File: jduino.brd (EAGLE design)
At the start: 100 x 80 mm, 20 parts, among them IC1 7805T, IC2 ATMEGA48/88/168-PU, Q1 16 mHz

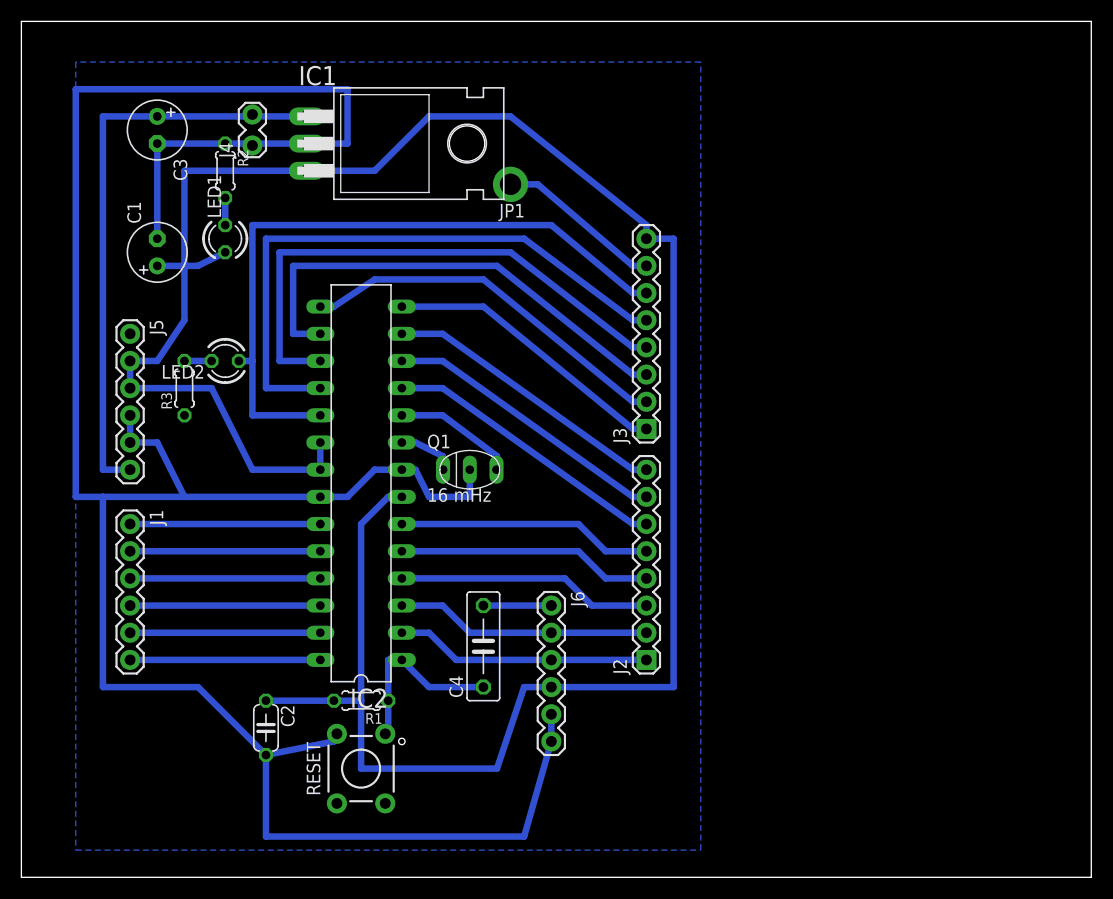
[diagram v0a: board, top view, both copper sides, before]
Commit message: Added power elements.
Added a protection diode and a power switch. Also swapped out the
7805 for a LDO regulator.
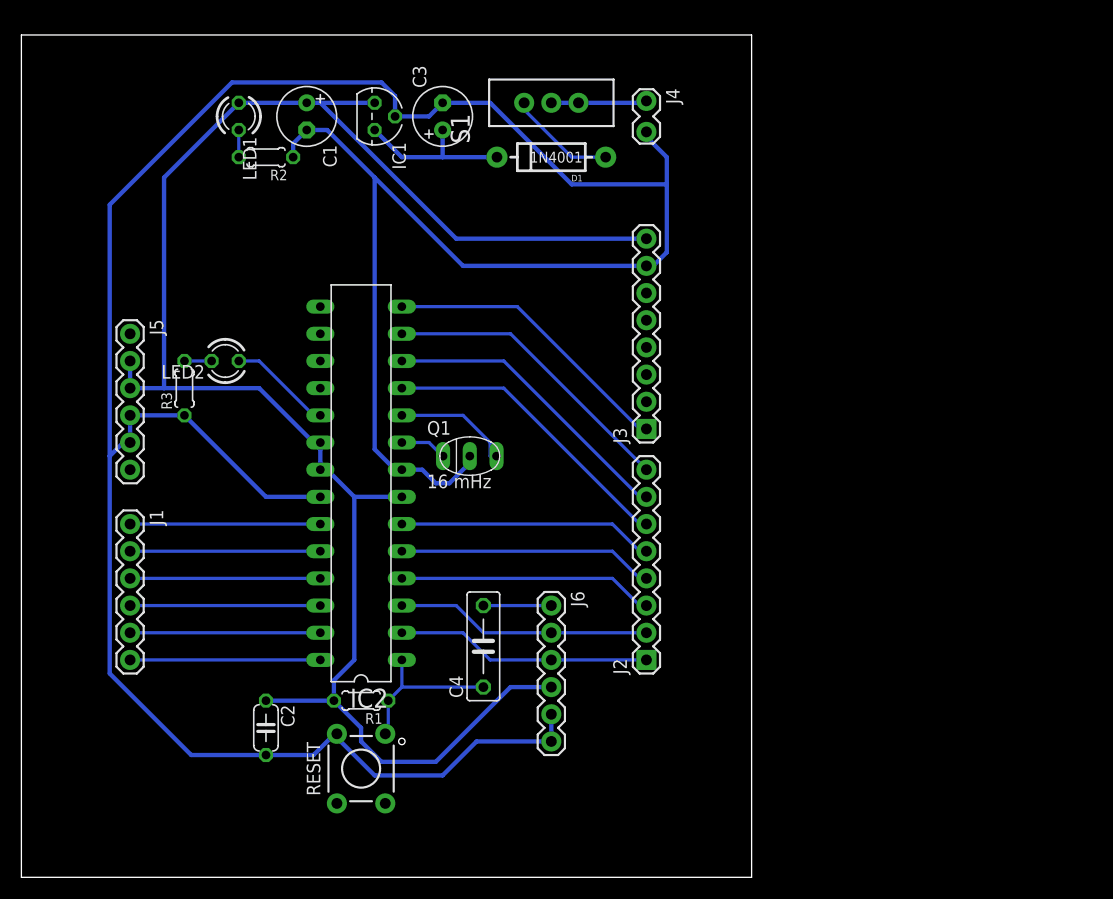
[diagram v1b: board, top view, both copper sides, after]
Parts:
- removed JP1: M01PTH_2MM, SparkFun:1X01_2MM
- added D1: 1N4001, SparkFun-DiscreteSemi:DIODE-1N4001
- added S1: power, SparkFun-Electromechanical:SWITCH-SPDT
- IC1: value 7805T -> LM2936Z-5.0; device linear:TO220H -> national-semiconductor:TO92
- J4: value (none) -> 6V - 30V in
- R2: value 330ohm -> 330
- moved J4 37.0 mm to (58.4, 72.4), turned to 270 degrees
- moved C3 26.7 mm to (39.4, 71.1), turned to 90 degrees
- moved C1 18.9 mm to (26.7, 71.1), turned to 270 degrees
- moved LED1 11.5 mm to (20.3, 71.1), turned to 270 degrees
- moved IC1 4.58 mm to (33.0, 71.1)
- moved R2 4.02 mm to (22.9, 67.3), turned to 180 degrees
- moved Q1 1.27 mm to (41.9, 39.4)
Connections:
- new net N$6: C3.+, D1.C, IC1.3
- new net N$7: D1.A, S1.1
- net +5V: now also IC1.1; no longer IC1.3
- net GND: now also J3.7, J4.2; no longer J4.1
- net N$1: now also J5.1
- net N$2: now also J4.1, S1.2, S1.3; no longer J3.7, JP1.1
- net VIN: no longer C3.+, IC1.1, J4.2
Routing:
- net D12: track 57.2 -> 0.00 mm
- net +5V: track 221.2 -> 164.7 mm
- net D13: track 64.5 -> 9.72 mm
- net VIN: track 54.8 -> 0.00 mm
- net D11: track 51.3 -> 0.00 mm
- net D10: track 45.5 -> 0.00 mm
- net GND: track 234.6 -> 275.2 mm
- net D9: track 35.3 -> 0.00 mm
- net N$6: track 0.00 -> 15.0 mm
- net N$7: track 0.00 -> 10.1 mm
- net N$2: track 15.5 -> 9.07 mm
- net RESET: track 16.9 -> 15.1 mm
- net D6: track 26.9 -> 28.1 mm
- net D5: track 26.9 -> 28.1 mm
- net D7: track 26.9 -> 28.1 mm
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- removed copper zone on layer 16, net GND
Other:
- board size 100 x 80 mm -> 68.2 x 78.7 mm

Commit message: Initial complete version.
Routed D9 - D13, GND, and AREF to the headers. Rotated the FTDI
header to be able to use a right angle header. Two jumpers remain.
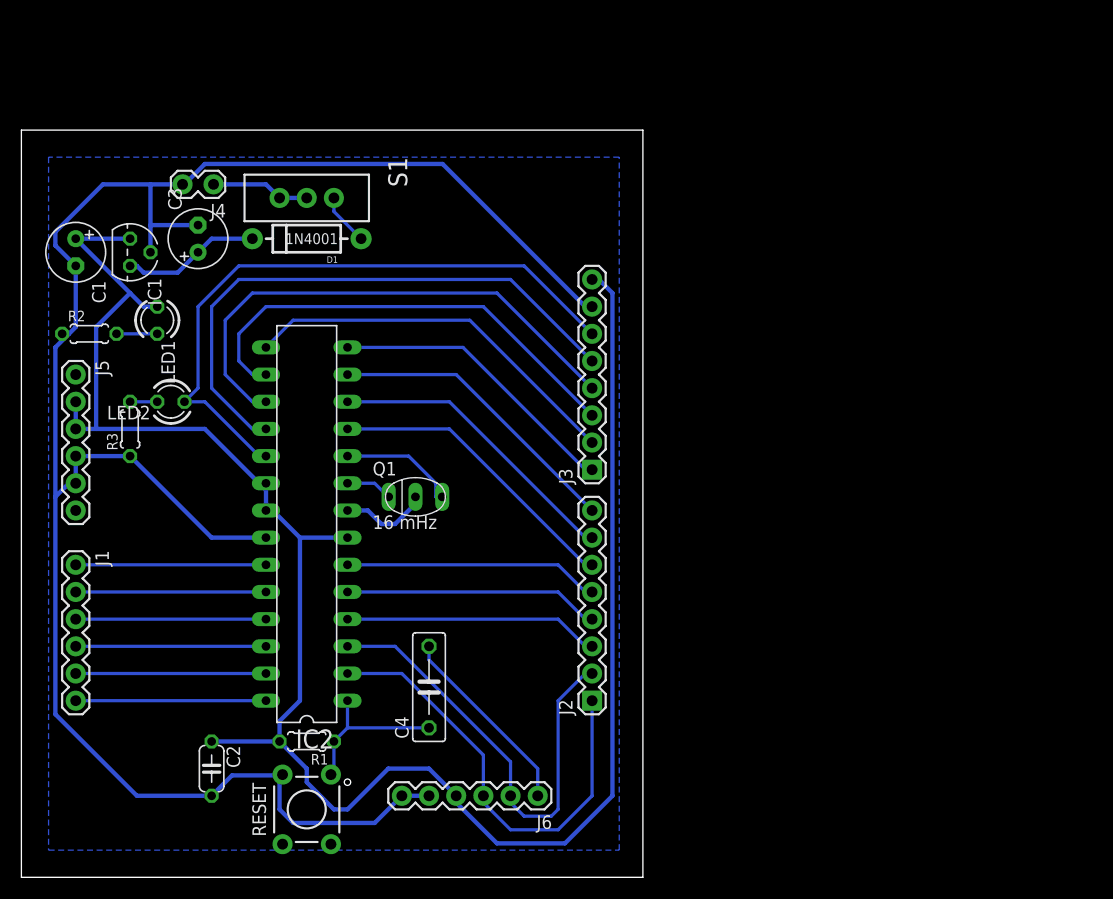
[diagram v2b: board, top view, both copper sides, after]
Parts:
- moved J4 41.3 mm to (17.8, 64.8), turned to 180 degrees
- moved IC1 26.2 mm to (10.2, 58.4)
- moved C3 25.6 mm to (16.5, 59.7)
- moved C1 25.0 mm to (5.08, 58.4)
- moved S1 24.5 mm to (26.7, 63.5), turned to 270 degrees
- moved D1 24.1 mm to (26.7, 59.7)
- moved R2 23.3 mm to (6.35, 50.8), turned to 0 degrees
- moved LED1 20.5 mm to (12.7, 52.1)
- moved J6 17.8 mm to (48.3, 7.62), turned to 180 degrees
- moved J1 6.35 mm to (5.08, 29.2)
- moved R3 6.35 mm to (10.2, 41.9)
- moved R1 6.35 mm to (26.7, 12.7)
- moved C2 6.35 mm to (17.8, 10.2)
- moved RESET 6.35 mm to (26.7, 6.35)
- moved C4 6.35 mm to (38.1, 17.8)
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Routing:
- net GND: track 275.2 -> 196.0 mm
- net D12: track 0.00 -> 54.0 mm
- net D13: track 9.72 -> 60.2 mm
- net D11: track 0.00 -> 49.0 mm
- net D10: track 0.00 -> 43.9 mm
- net D9: track 0.00 -> 36.3 mm
- net D1: track 23.9 -> 43.1 mm
- net D0: track 23.9 -> 41.7 mm
- net +5V: track 164.7 -> 180.3 mm
- net N$1: track 6.35 -> 18.2 mm
- net N$7: track 10.1 -> 4.86 mm
- net N$6: track 15.0 -> 13.0 mm
- net N$26: track 2.54 -> 3.81 mm
- added copper zone on layer 16, net GND
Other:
- board size 68.2 x 78.7 mm -> 58.1 x 69.8 mm

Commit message: Replaced Euro-stype capacitors.
Replaced the large reset capacitors with smaller-package 0.1 uF
capacitors.
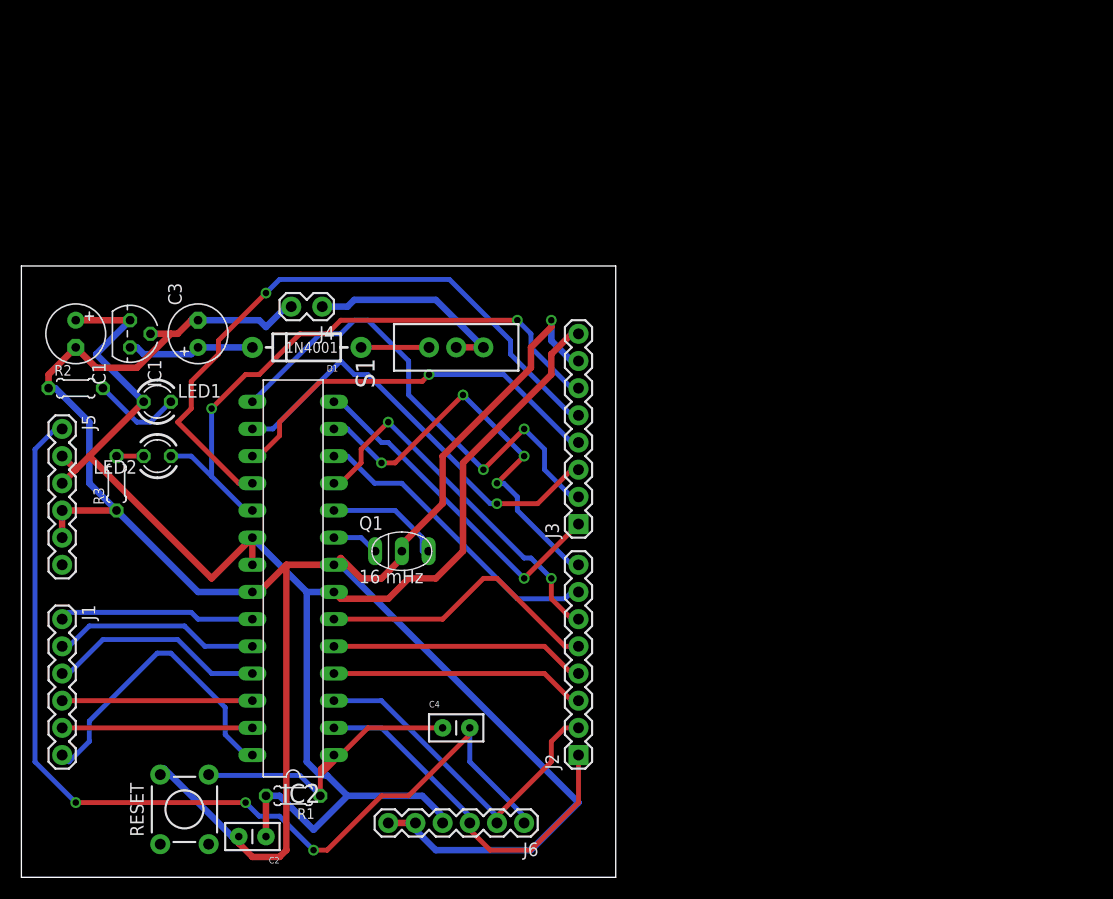
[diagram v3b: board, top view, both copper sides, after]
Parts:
- C2: value .1uf -> 0.1uF; device rcl:C050-024X044 -> SparkFun-Passives:CAP-PTH-SMALL2
- C4: value (none) -> 0.1uF; device rcl:C075-032X103 -> SparkFun-Passives:CAP-PTH-SMALL2
- moved S1 19.8 mm to (40.6, 49.5), turned to 90 degrees
- moved J4 15.3 mm to (27.9, 53.3)
- moved RESET 11.4 mm to (15.2, 6.35)
- moved D1 10.2 mm to (26.7, 49.5)
- moved C3 8.89 mm to (16.5, 50.8)
- moved C2 8.13 mm to (22.9, 3.81), turned to 180 degrees
- moved C1 7.62 mm to (5.08, 50.8)
- moved IC1 7.62 mm to (10.2, 50.8)
- moved LED1 7.62 mm to (12.7, 44.5), turned to 0 degrees
- moved LED2 5.24 mm to (12.7, 39.4)
- moved J5 5.24 mm to (3.81, 41.9)
- moved IC2 5.24 mm to (25.4, 27.9)
- moved J1 5.24 mm to (3.81, 24.1)
- moved J2 5.24 mm to (52.1, 11.4)
- moved Q1 5.24 mm to (35.6, 30.5)
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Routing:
- net N$1: track 18.2 -> 92.7 mm, vias 0 -> 3
- net +5V: track 180.3 -> 147.0 mm
- net GND: track 196.0 -> 214.5 mm, vias 0 -> 1
- net RESET: track 15.1 -> 28.8 mm
- net D11: track 49.0 -> 37.0 mm, vias 0 -> 1
- net D7: track 28.1 -> 39.2 mm, vias 0 -> 4
- net A5: track 17.8 -> 28.8 mm
- net N$2: track 9.24 -> 19.7 mm
- net D9: track 36.3 -> 46.6 mm, vias 0 -> 2
- net D1: track 43.1 -> 33.1 mm
- net D0: track 41.7 -> 34.6 mm
- net D5: track 28.1 -> 34.7 mm, vias 0 -> 2
- net D12: track 54.0 -> 60.6 mm, vias 0 -> 1
- net N$26: track 3.81 -> 8.45 mm
- net D8: track 27.6 -> 31.8 mm, vias 0 -> 1
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- removed copper zone on layer 16, net GND
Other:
- board size 58.1 x 69.8 mm -> 55.5 x 57.1 mm

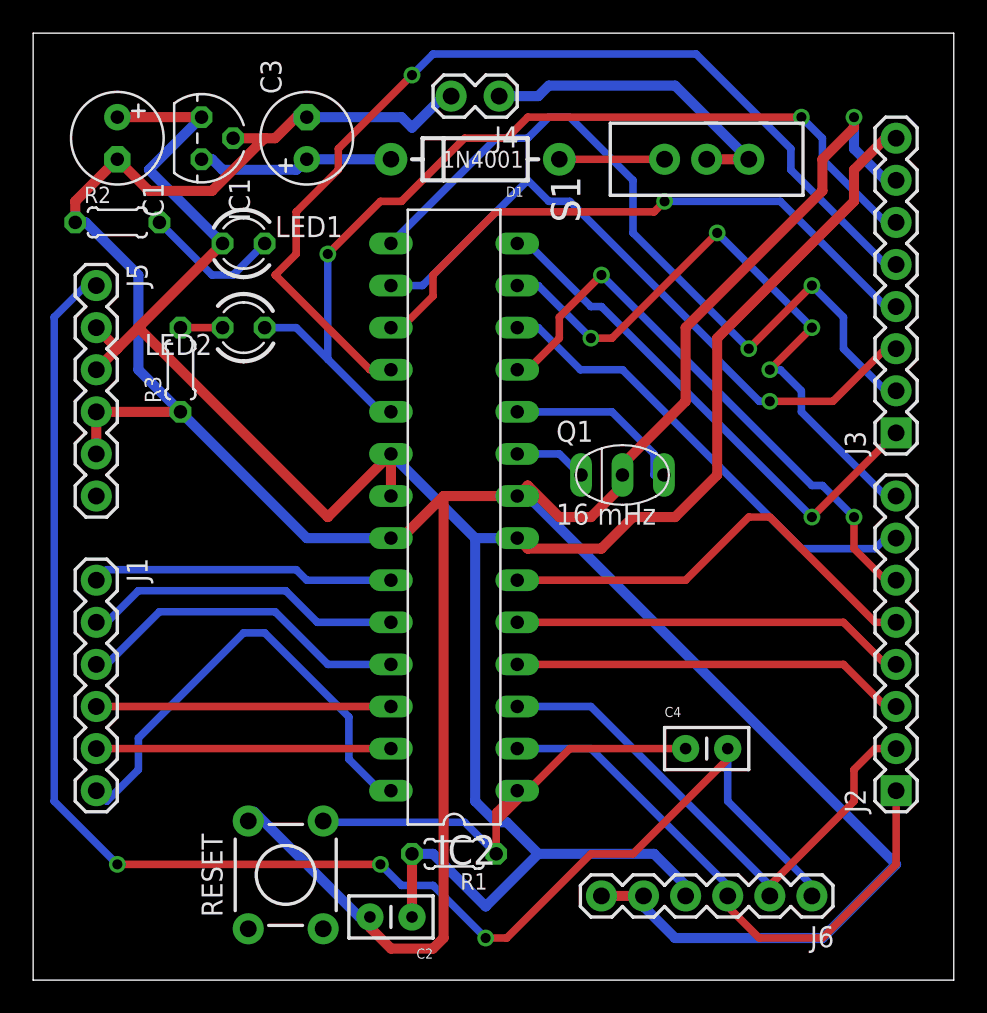
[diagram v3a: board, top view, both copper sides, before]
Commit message: Hand routed some pins.
I hand-routed pins 3 through 5 and 23 through 28, since these should
be straight-shots. Then auto routed the remaining traces. The board
still needs significant cleanup.
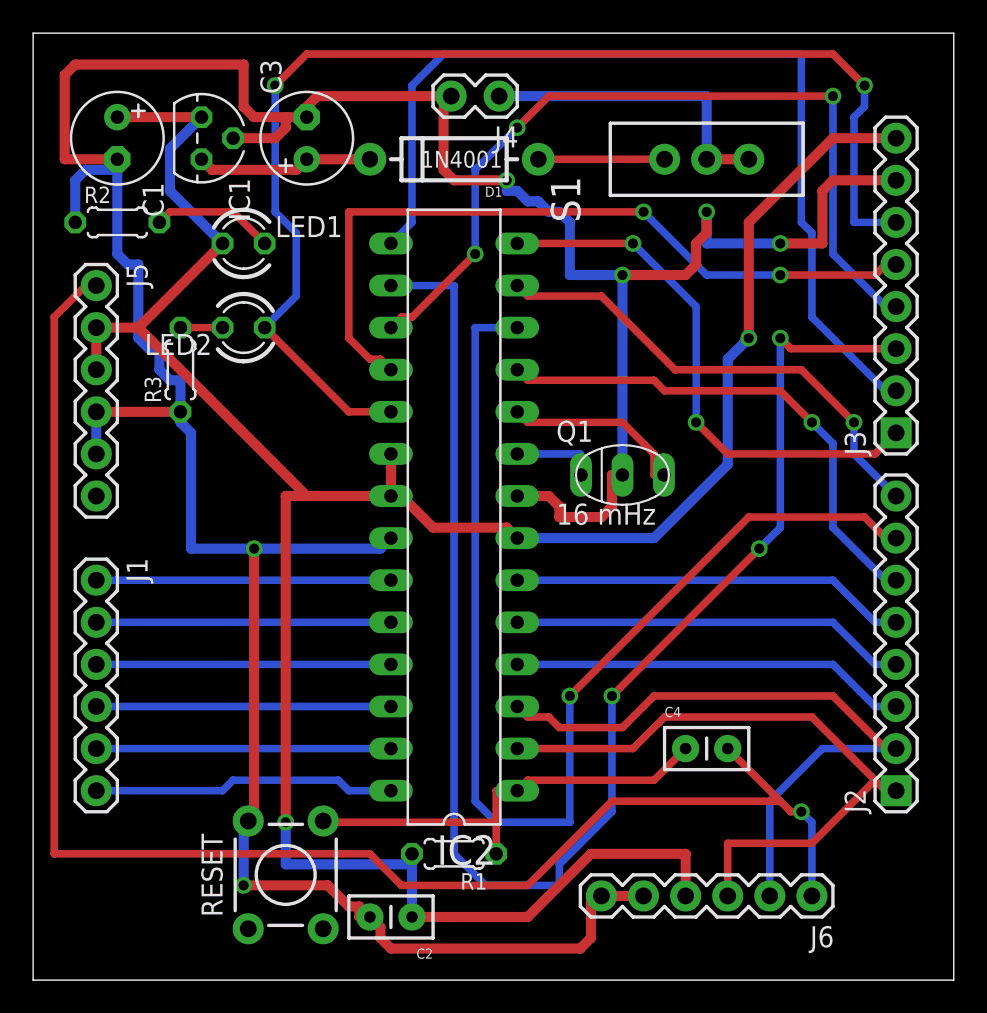
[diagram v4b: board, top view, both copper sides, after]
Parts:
- moved D1 1.27 mm to (25.4, 49.5)
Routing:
- net D10: track 40.3 -> 91.0 mm, vias 1 -> 3
- net D6: track 28.6 -> 69.7 mm, vias 0 -> 1
- net D13: track 57.2 -> 73.8 mm
- net D12: track 60.6 -> 45.8 mm, vias 1 -> 2
- net D11: track 37.0 -> 50.1 mm, vias 1 -> 3
- net D9: track 46.6 -> 57.4 mm, vias 2 -> 0
- net A5: track 28.8 -> 18.3 mm
- net D7: track 39.2 -> 29.2 mm, vias 4 -> 1
- net D1: track 33.1 -> 40.1 mm
- net +5V: track 147.0 -> 153.9 mm, vias 0 -> 2
- net GND: track 214.5 -> 207.7 mm, vias 1 -> 6
- net D0: track 34.6 -> 39.1 mm
- net D5: track 34.7 -> 31.1 mm, vias 2 -> 1
- net D4: track 27.1 -> 23.9 mm
- net A2: track 20.4 -> 17.8 mm
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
